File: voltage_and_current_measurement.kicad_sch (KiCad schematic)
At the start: 62 parts

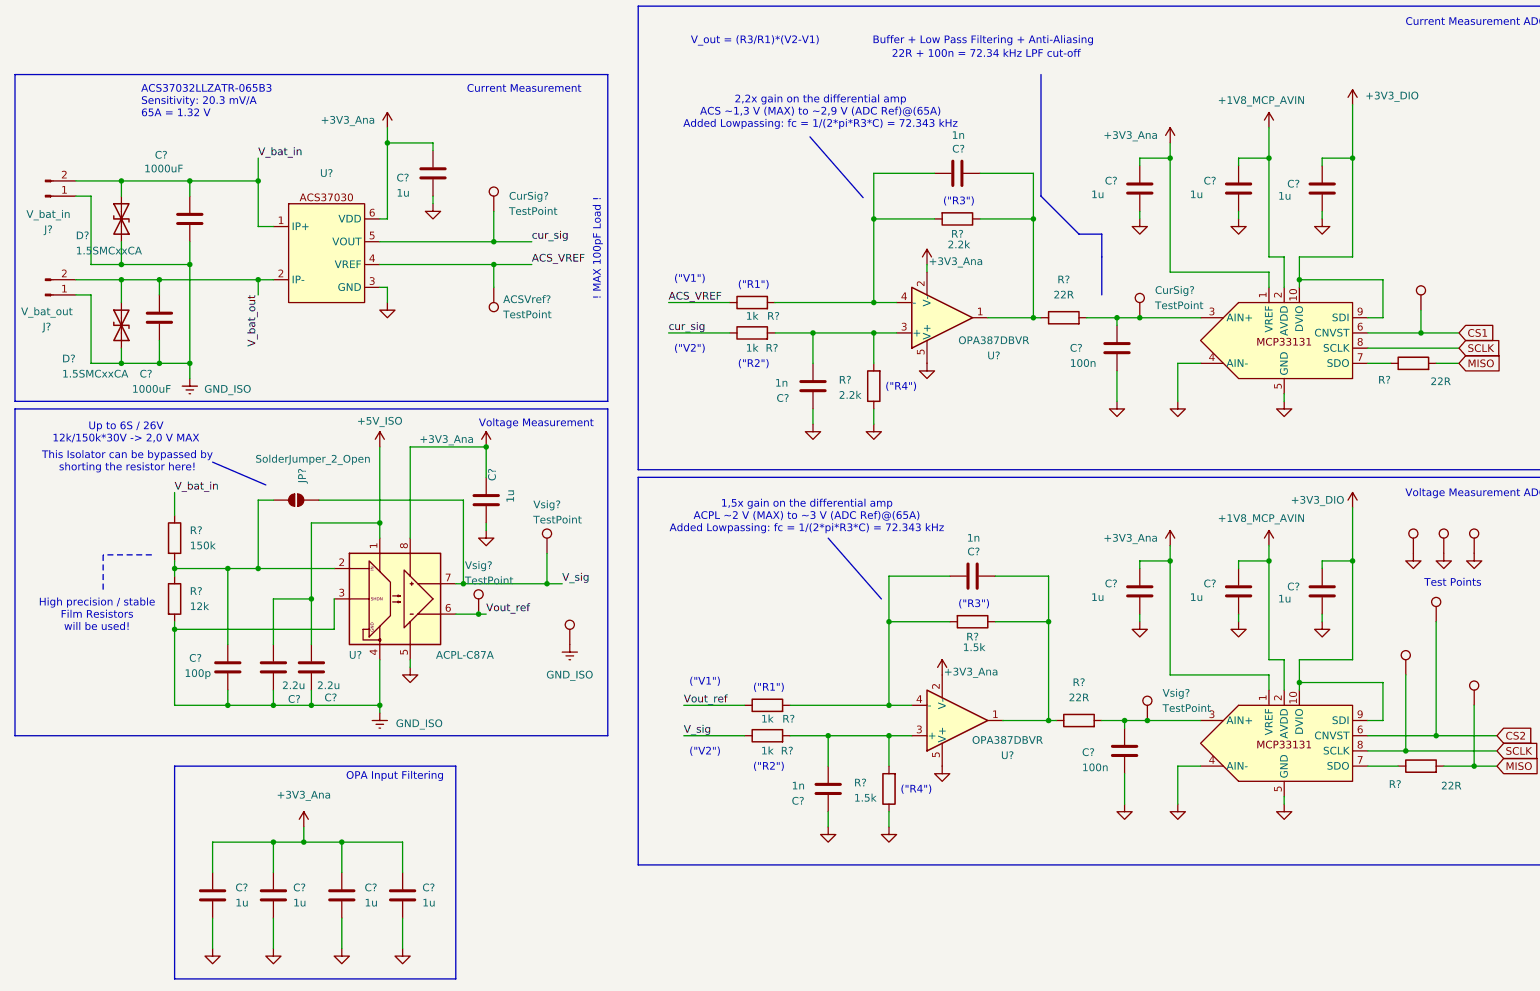
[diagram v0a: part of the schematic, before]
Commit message: Add proper Load Cell ADC. Improve everything. Almost ready.
[KiCad Version: 9.0.8]
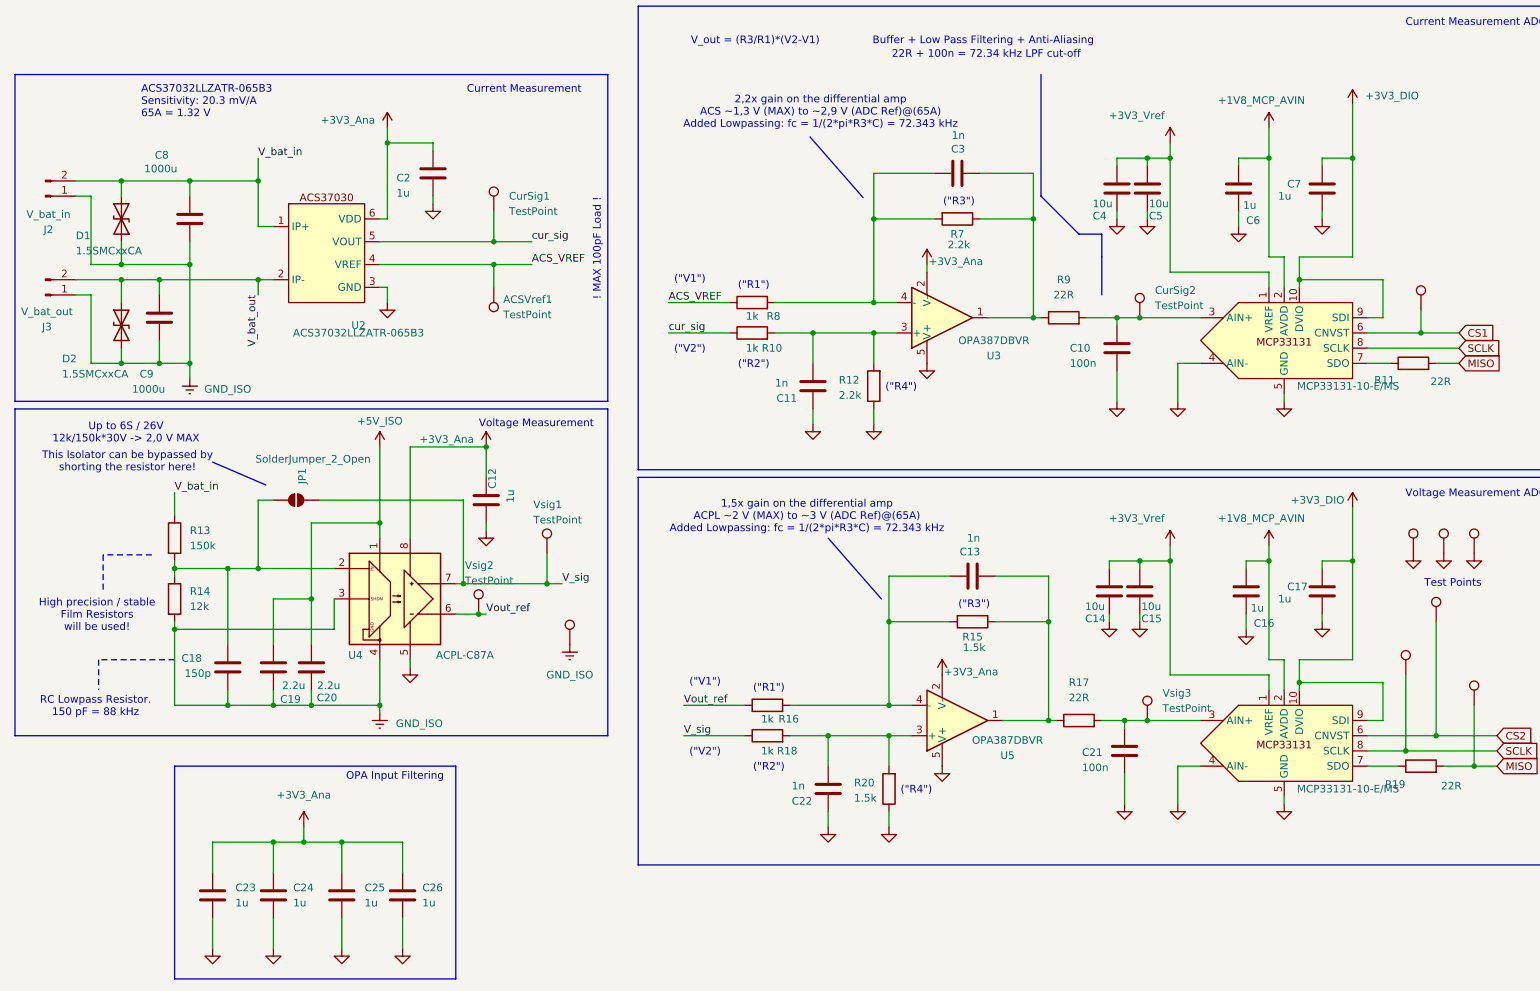
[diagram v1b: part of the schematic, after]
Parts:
- removed C? (x3): 1u, Capacitor_SMD:C_0603_1608Metric_Pad1.08x0.95mm_HandSolder, symbol Device:C
- added C14, C15, C5: 10u, Capacitor_SMD:C_0603_1608Metric_Pad1.08x0.95mm_HandSolder, symbol Device:C
- added C16, C6: 1u, Capacitor_SMD:C_0603_1608Metric_Pad1.08x0.95mm_HandSolder, symbol Device:C
- C18: renamed from C?; value 100p -> 150p
- C4: renamed from C?; value 1u -> 10u
- C8, C9: renamed from C?; value 1000uF -> 1000u
- MCP1, MCP2: renamed from MCP?; value ~ -> MCP33131-10-E/MS; Manufacturing_Number (none) -> MCP33131-10-E/MS
- U2: renamed from U?; value ~ -> ACS37032LLZATR-065B3; Manufacturing_Number (none) -> ACS37032LLZATR-065B3
- gave numbers to parts that had none: 52
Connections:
- net +1V8_MCP_AVIN: now also C16.2, C6.2
- net +3V3_Ana: no longer C4.1, MCP1.1 (VREF), MCP2.1 (VREF)
- net GND: now also C14.2, C15.2, C16.1, C5.2, C6.1
- new net +3V3_Vref: C14.1, C15.1, C4.1, C5.1, MCP1.1 (VREF), MCP2.1 (VREF)
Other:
- note added: "RC Lowpass Resistor. 150 pF = 88 kHz"
- moved on the sheet: C4

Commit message: Switched isolating opamp. Switched Isolating DCDC converter. Minor layout improvements. Added load cell ADC.
[KiCad Version: 10.0.4]
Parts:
- removed C12: 1u, Capacitor_SMD:C_0603_1608Metric_Pad1.08x0.95mm_HandSolder, symbol Device:C
- removed C18: 150p, Capacitor_SMD:C_0603_1608Metric_Pad1.08x0.95mm_HandSolder, symbol Device:C
- removed C19, C20: 2.2u, Capacitor_SMD:C_0603_1608Metric_Pad1.08x0.95mm_HandSolder, symbol Device:C
- removed GND4: TestPoint, TestPoint:TestPoint_Pad_D1.0mm, symbol Connector:TestPoint
- removed JP1: SolderJumper_2_Open, Jumper:SolderJumper-2_P1.3mm_Open_RoundedPad1.0x1.5mm, symbol Jumper:SolderJumper_2_Open
- removed R13: 150k, Resistor_SMD:R_0603_1608Metric_Pad0.98x0.95mm_HandSolder, symbol Device:R
- removed R14: 12k, Resistor_SMD:R_0603_1608Metric_Pad0.98x0.95mm_HandSolder, symbol Device:R
- removed U4: ACPL-C87A, Package_SO:SSO-8_6.8x5.9mm_P1.27mm_Clearance8mm, symbol Isolator_Analog:ACPL-C87A
- added C13, C15, C3, C35, C36, C4, C5, C6: 1u, Capacitor_SMD:C_0603_1608Metric_Pad1.08x0.95mm_HandSolder, symbol Device:C
- added C2: 330p, Capacitor_SMD:C_0603_1608Metric_Pad1.08x0.95mm_HandSolder, symbol Device:C
- added C30, C31: 1n, Capacitor_SMD:C_0603_1608Metric_Pad1.08x0.95mm_HandSolder, symbol Device:C
- added C32, C34: 10u, Capacitor_SMD:C_0603_1608Metric_Pad1.08x0.95mm_HandSolder, symbol Device:C
- added C33: 100n, Capacitor_SMD:C_0603_1608Metric_Pad1.08x0.95mm_HandSolder, symbol Device:C
- added CS3, CurSig3, GND1: TestPoint, TestPoint:TestPoint_Pad_D1.0mm, symbol Connector:TestPoint
- added IC1: VIA2000SD, SOIC127P1150X280-8N, symbol SamacSys_Parts:VIA2000SD
- added IC2, IC3: OPA2387DR, SOIC127P600X175-8N, symbol SamacSys_Parts:OPA2387DR
- added MCP3: MCP33131-10-E/MS, Package_SO:MSOP-10_3x3mm_P0.5mm, symbol Custom Symbols:MCP33131
- added R19, R20: 1k, Resistor_SMD:R_0603_1608Metric_Pad0.98x0.95mm_HandSolder, symbol Device:R
- added R21, R22: 2.2k, Resistor_SMD:R_0603_1608Metric_Pad0.98x0.95mm_HandSolder, symbol Device:R
- added R23, R24: 22R, Resistor_SMD:R_0603_1608Metric_Pad0.98x0.95mm_HandSolder, symbol Device:R
- added R5: 15k, Resistor_SMD:R_0603_1608Metric_Pad0.98x0.95mm_HandSolder, symbol Device:R
- added R6: 1.2k, Resistor_SMD:R_0603_1608Metric_Pad0.98x0.95mm_HandSolder, symbol Device:R
- added U5: OPA387DBVR, Package_TO_SOT_SMD:SOT-23-5, symbol Amplifier_Operational:OPA310xDBV
- U2: value ACS37032LLZATR-065B3 -> ACS37030LLZATR-065B3; Manufacturing_Number ACS37032LLZATR-065B3 -> ACS37030LLZATR-065B3
- renumbered C24 to C10, C25 to C11, C26 to C12, C2 to C14, C11 to C16, C22 to C17, C3 to C18, C13 to C19, C14 to C20, C4 to C21, C10 to C22, C21 to C23, C15 to C24, C5 to C25, C6 to C26, C16 to C27, C7 to C28, C17 to C29, C9 to C7, C23 to C9, GND1 to GND2, GND2 to GND3, GND3 to GND4, J2 to J3, J3 to J4, R18 to R10, R12 to R11, R20 to R12, R7 to R13, R15 to R14, R9 to R15, R17 to R16, R11 to R17, R19 to R18, R8 to R7, R10 to R8, R16 to R9, U5 to U4
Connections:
- net +1V8_MCP_AVIN: now also C35.2, MCP3.2 (AVDD)
- net +3V3_Ana: now also C13.1, C15.1, C5.1, C6.1, IC1.8 (VDD2), U5.2 (V-)
- net +3V3_DIO: now also C36.1, MCP3.10 (DVIO), MCP3.9 (SDI)
- net +3V3_Vref: now also C32.1, C34.1, MCP3.1 (VREF)
- net ACS_VREF: now also R19.1
- net CS1: now also CS3.1, MCP3.6 (CNVST)
- net GND: now also C13.2, C15.2, C3.2, C30.1, C32.2, C33.2, C34.2, C35.1, C36.2, C4.2, C5.2, C6.2, IC1.5 (GND2), MCP3.4 (AIN-), MCP3.5 (GND), R21.1, U5.5 (V+)
- net GND_ISO: now also C2.2, GND1.1, IC1.3 (SHTDN), IC1.4 (GND1), R6.2
- net MISO: now also R24.2
- net SCLK: now also MCP3.8 (SCLK)
- net V_bat_in: now also R5.1
- net V_sig: now also IC1.7 (OUTP)
- net Vout_ref: now also IC1.6 (OUTN)
- net cur_sig: now also R20.1
- new net: C33.1, CurSig3.1, MCP3.3 (AIN+), R23.2
- new net: C31.2, R22.1, R23.1, U5.1
- new net: C31.1, R19.2, R22.2, U5.4 (-)
- new net: MCP3.7 (SDO), R24.1
- new net: C30.2, R20.2, R21.2, U5.3 (+)
- new net: C2.1, IC1.2 (VIN), R5.2, R6.1
- new net +3V3_ISO: C3.1, C4.1, IC1.1 (VDD1)
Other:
- note added: "ACS37030LLZATR-065B3 Sensitivity: 20.3 mV/A 65A = 1.32 V"
- note added: "LAITA 3 tai 4 KANAVAINEN LOAD CELL ADC JOLLOIN VOIDAAN LISÄTÄ LÄMPÖMITTAREITA TUOHON PIIRILEVYLLE MITTAAMAAN KAIKKEA !?"
- note added: "LAITE EI VOI MITATA PIENIÄ VIRTOJA KOSKA TUO EI OLE TRUE RAIL TO RAIL !?"
- note added: "LASKE TUO 22R JA 100nF KONKAN LATAUS-AIKA !? ONKO TUO R22 LIIKAA?"
- note added: "RC Lowpass Resistor. 330 pF = 423 kHz (@-3dB)"
- note added: "TARKASTA KUMPI ACS VERSIO ON TUO VREF / FAULT !!!!!!"
- note added: "TODO:"
- note added: "TOTEUTA TUO JÄYKKÄ VREF SYÖTTÖ OPARILLA !?"
- note removed: "ACS37032LLZATR-065B3 Sensitivity: 20.3 mV/A 65A = 1.32 V"
- note removed: "RC Lowpass Resistor. 150 pF = 88 kHz"
- note removed: "This Isolator can be bypassed by shorting the resistor here!"
- note removed: "Voltage Measurement"
- moved on the sheet: C10, C11, C12, C9

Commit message: Implemented proper sallen key filter. Add 4V2 LDO Back.
[KiCad Version: 10.0.4]
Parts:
- removed C10, C12, C35, C36, C9: 1u, Capacitor_SMD:C_0603_1608Metric_Pad1.08x0.95mm_HandSolder, symbol Device:C
- removed C30, C31: 1n, Capacitor_SMD:C_0603_1608Metric_Pad1.08x0.95mm_HandSolder, symbol Device:C
- removed C32, C34: 10u, Capacitor_SMD:C_0603_1608Metric_Pad1.08x0.95mm_HandSolder, symbol Device:C
- removed C33: 100n, Capacitor_SMD:C_0603_1608Metric_Pad1.08x0.95mm_HandSolder, symbol Device:C
- removed CS3, CurSig2, CurSig3, Vsig3: TestPoint, TestPoint:TestPoint_Pad_D1.0mm, symbol Connector:TestPoint
- removed IC2, IC3: OPA2387DR, SOIC127P600X175-8N, symbol SamacSys_Parts:OPA2387DR
- removed MCP3: MCP33131-10-E/MS, Package_SO:MSOP-10_3x3mm_P0.5mm, symbol Custom Symbols:MCP33131
- removed R19, R20: 1k, Resistor_SMD:R_0603_1608Metric_Pad0.98x0.95mm_HandSolder, symbol Device:R
- removed R21, R22: 2.2k, Resistor_SMD:R_0603_1608Metric_Pad0.98x0.95mm_HandSolder, symbol Device:R
- removed R23, R24: 22R, Resistor_SMD:R_0603_1608Metric_Pad0.98x0.95mm_HandSolder, symbol Device:R
- removed U3, U4, U5: OPA387DBVR, Package_TO_SOT_SMD:SOT-23-5, symbol Amplifier_Operational:OPA310xDBV
- added C13, C14, C15: 100pF, Capacitor_SMD:C_0603_1608Metric_Pad1.08x0.95mm_HandSolder, symbol Device:C
- added C20, C21: 205pF, Capacitor_SMD:C_0603_1608Metric_Pad1.08x0.95mm_HandSolder, symbol Device:C
- added C24, C25: 1.7nF, Capacitor_SMD:C_0603_1608Metric_Pad1.08x0.95mm_HandSolder, symbol Device:C
- added R15, R18: 22R, Resistor_SMD:R_0603_1608Metric_Pad0.98x0.95mm_HandSolder, symbol Device:R
- added U3, U4: OPA2328DR, Package_SO:SOIC-8_3.9x4.9mm_P1.27mm, symbol Amplifier_Operational:OPA2325
- C16: value 1n -> 100pF
- C17: value 1n -> 1u
- C18, C19: value 1n -> 205pF
- C22, C23: value 100n -> 1.7nF
- MCP1, MCP2: value MCP33131-10-E/MS -> MCP33131D-10-E/MS
- R10, R7, R8, R9: value 1k -> 2.37k
- R11, R13: value 2.2k -> 3.32k
- R12, R14: value 1.5k -> 3.32k
- renumbered C5 to C10, C6 to C11, C11 to C12, C7 to C2, C20 to C26, C21 to C27, C24 to C28, C25 to C29, C8 to C3, C26 to C30, C27 to C31, C28 to C32, C29 to C33, C2 to C4, C3 to C5, C4 to C6, C13 to C7, C14 to C8, C15 to C9, J3 to J4, J4 to J5, R15 to R17, R17 to R19, R18 to R20
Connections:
- net +3V3_Ana: now also C17.1, U3.8 (V+), U4.8 (V+)
- net ACS_VREF: now also R8.1; no longer R7.1
- net GND: now also C16.2, C17.2, C13.2, C14.2, C15.2, C24.2, C25.2, U3.4 (V-), U4.4 (V-); no longer C16.1, C17.1, C5.2, C6.2, MCP1.4 (AIN-), MCP2.4 (AIN-), R11.1, R12.1
- net GND_ISO: now also C5.2, C6.2
- net V_sig: now also R9.1; no longer R10.1
- net Vout_ref: now also R10.1; no longer R9.1
- net cur_sig: now also R7.1; no longer R8.1
- net at C18.2, R17.1: now also U3.1, U3.2 (-); no longer R13.1
- net at C18.1, R7.2: now also R11.1; no longer R13.2
- net +3V3_Vref renamed +3V_Vref
- new net: C19.1, R12.1, R8.2
- new net: C20.1, R13.1, R9.2
- new net: C15.1, R13.2, U4.3 (+)
- new net: C23.1, MCP1.4 (AIN-), R15.2
- new net: C13.1, R11.2, U3.3 (+)
- new net: C19.2, R15.1, U3.6 (-), U3.7
- new net: C14.1, R12.2, U3.5 (+)
- new net: C25.1, MCP2.4 (AIN-), R16.2
- new net: C21.2, R16.1, U4.6 (-), U4.7
- new net: C20.2, R18.1, U4.1, U4.2 (-)
- new net: C24.1, MCP2.3 (AIN+), R18.2
- new net: C21.1, R10.2, R14.1
- new net: C16.1, R14.2, U4.5 (+)
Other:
- note added: "Buffer + Low Pass Filtering + Anti-Aliasing / SAR Charge Bucket"
- note added: "Fully differential Sallen-Key Buffering: -400 kHz Butterworth cut-off freq, Q=0.706, GBWreq=28.284 M, Gain=1 -Dimensioned with: https://webench.ti.com/filter-design-tool/ -22R + 1.7nF charge bucket from MCP33131D datasheet"
- note added: "Isolated Voltage Measurement"
- note added: "OPA Annalog Supply"
- note removed: "("R1")"
- note removed: "("R2")"
- note removed: "("R3")"
- note removed: "("R4")"
- note removed: "("V1")"
- note removed: "("V2")"
- note removed: "1,5x gain on the differential amp ACPL ~2 V (MAX) to ~3 V (ADC Ref)@(65A) Added Lowpassing: fc = 1/(2*pi*R3*C) = 72.343 kHz"
- note removed: "2,2x gain on the differential amp ACS ~1,3 V (MAX) to ~2,9 V (ADC Ref)@(65A) Added Lowpassing: fc = 1/(2*pi*R3*C) = 72.343 kHz"
- note removed: "22R + 100n = 72.34 kHz LPF cut-off"
- note removed: "Buffer + Low Pass Filtering + Anti-Aliasing"
- note removed: "OPA Input Filtering"
- note removed: "V_out = (R3/R1)*(V2-V1)"
- moved on the sheet: ACSVref1, C10, C11, C12, C2, C22, C26, C27, C28, C29, C3, C30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

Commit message: Quite final version with ACS current sensor.
[KiCad Version: 10.0.4]
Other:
- note removed: "LAITA 3 tai 4 KANAVAINEN LOAD CELL ADC JOLLOIN VOIDAAN LISÄTÄ LÄMPÖMITTAREITA TUOHON PIIRILEVYLLE MITTAAMAAN KAIKKEA !?"
- note removed: "LAITE EI VOI MITATA PIENIÄ VIRTOJA KOSKA TUO EI OLE TRUE RAIL TO RAIL !?"
- note removed: "LASKE TUO 22R JA 100nF KONKAN LATAUS-AIKA !? ONKO TUO R22 LIIKAA?"
- note removed: "TODO:"
- note removed: "TOTEUTA TUO JÄYKKÄ VREF SYÖTTÖ OPARILLA !?"
- moved on the sheet: C12, C17, U3C, U4C

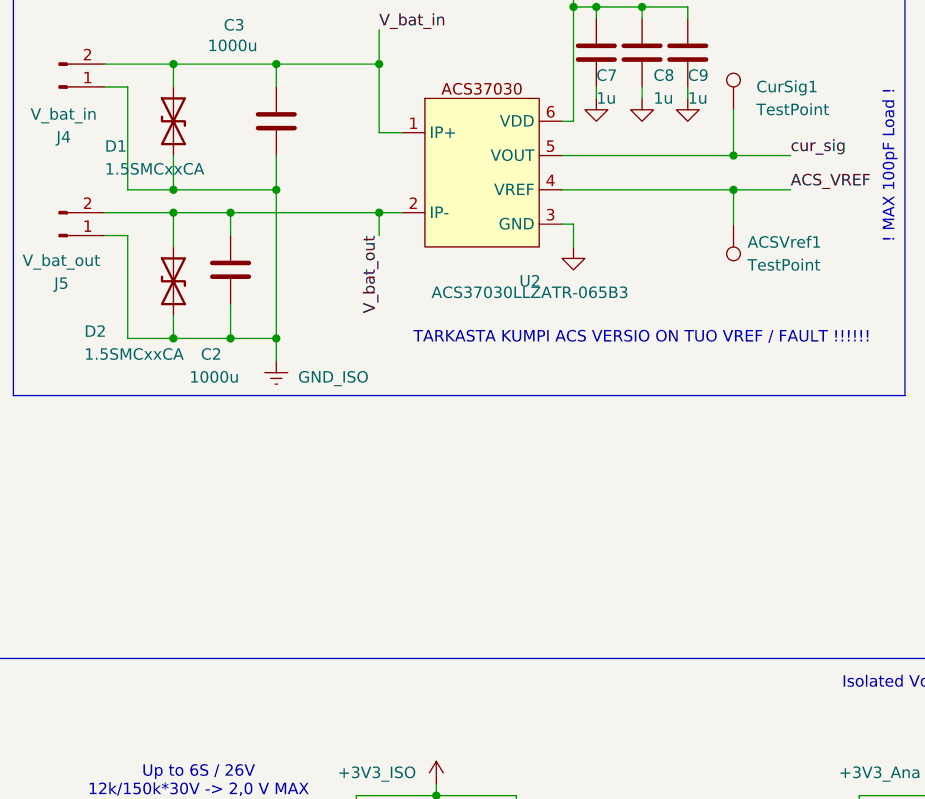
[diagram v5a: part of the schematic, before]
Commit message: Start adding new current sensor
[KiCad Version: 10.0.4]
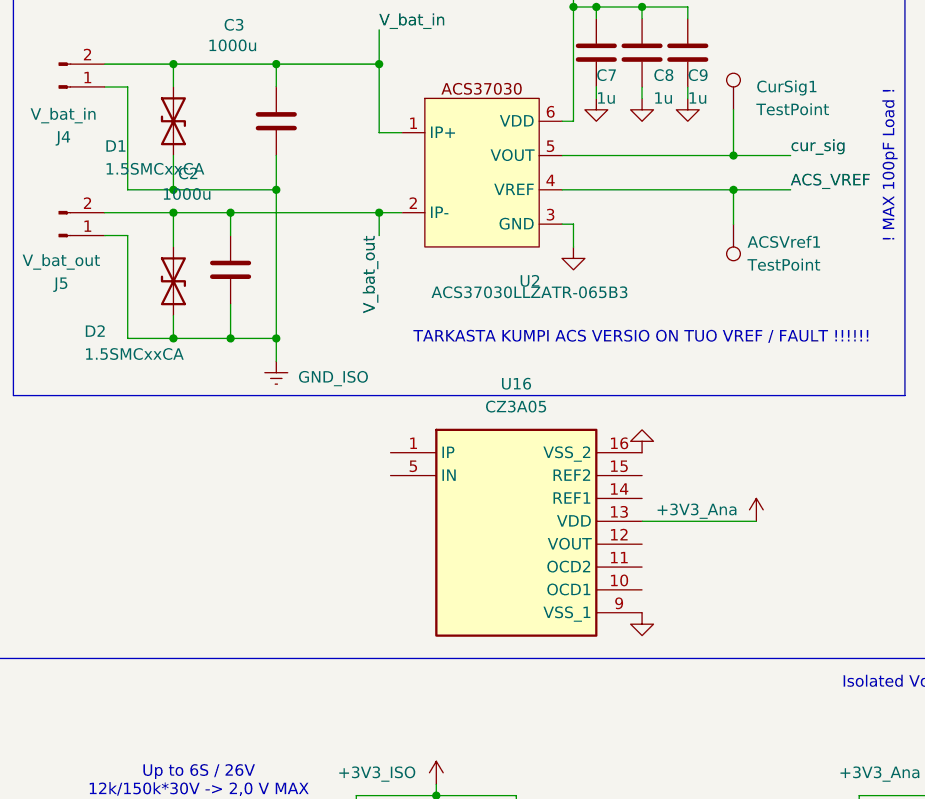
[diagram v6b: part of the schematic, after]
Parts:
- added U16: CZ3A05, CZ3A05, symbol SamacSys_Parts:CZ3A05
- C2, C3: footprint Capacitor_THT:CP_Radial_D12.5mm_P5.00mm -> Capacitor_THT:C_Radial_D8.0mm_H11.5mm_P3.50mm
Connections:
- net +3V3_Ana: now also U16.13 (VDD)
- net GND: now also U16.16 (VSS_2), U16.9 (VSS_1)
